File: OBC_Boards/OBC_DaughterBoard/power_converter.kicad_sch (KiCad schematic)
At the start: 12 parts, among them Q1 Q_PMOS_DGS, U2 BU33SA5WGWZ-E2-qsat-symb

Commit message: obc: daughterboard: clean up all schematics for easier reworks
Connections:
- net 3V3: no longer names the net of FB3.1
- net 5V_Rpi_Input: no longer names the net of FB2.2
- net Analog_Voltage: no longer names the net of R7.2, R8.2
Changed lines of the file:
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@@
+    (stroke (width 0) (type default) (color 0 0 0 0))
+  )
+  (wire (pts (xy 101.6 84.455) (xy 109.22 84.455))
     (stroke (width 0) (type default) (color 0 0 0 0))
   )
@@
     (stroke (width 0) (type default) (color 0 0 0 0))
   )
+  (wire (pts (xy 187.96 87.63) (xy 194.945 87.63))
+    (stroke (width 0) (type default) (color 0 0 0 0))
+  )
   (wire (pts (xy 150.114 87.884) (xy 150.114 88.9))
     (stroke (width 0) (type default) (color 0 0 0 0))
@@
   )
   (wire (pts (xy 137.16 95.504) (xy 137.16 98.806))
+    (stroke (width 0) (type default) (color 0 0 0 0))
+  )
+  (wire (pts (xy 194.945 80.01) (xy 194.945 87.63))
     (stroke (width 0) (type default) (color 0 0 0 0))
   )
@@
     (stroke (width 0) (type default) (color 0 0 0 0))
   )
-  (wire (pts (xy 105.918 84.074) (xy 109.22 84.074))
-    (stroke (width 0) (type default) (color 0 0 0 0))
-  )
   (wire (pts (xy 154.686 110.744) (xy 154.686 115.824))
     (stroke (width 0) (type default) (color 0 0 0 0))
   )
   (wire (pts (xy 159.004 91.694) (xy 159.004 94.488))
+    (stroke (width 0) (type default) (color 0 0 0 0))
+  )
+  (wire (pts (xy 101.6 84.455) (xy 101.6 83.82))
     (stroke (width 0) (type default) (color 0 0 0 0))
   )
@@
     (stroke (width 0) (type default) (color 0 0 0 0))
   )
-  (global_label "3V3" (shape input) (at 185.42 87.884 270) (fields_autoplaced)
+  (hierarchical_label "5V0_Input" (shape input) (at 101.6 83.82 180)
     (effects (font (size 1.27 1.27)) (justify right))
-    (property "Intersheet References" "${INTERSHEET_REFS}" (id 0) (at 185.3406 93.8047 90)
-      (effects (font (size 1.27 1.27)) (justify right) hide)
-    )
   )
-  (global_label "5V_Rpi_Input" (shape input) (at 105.918 84.074 180) (fields_autoplaced)
-    (effects (font (size 1.27 1.27)) (justify right))
-    (property "Intersheet References" "${INTERSHEET_REFS}" (id 0) (at 91.4701 83.9946 0)
-      (effects (font (size 1.27 1.27)) (justify right) hide)
-    )
-  )
-  (global_label "Analog_Voltage" (shape input) (at 165.608 110.744 0) (fields_autoplaced)
+  (hierarchical_label "Analog Output Voltage" (shape input) (at 165.735 110.49 0)
     (effects (font (size 1.27 1.27)) (justify left))
-    (property "Intersheet References" "${INTERSHEET_REFS}" (id 0) (at 182.354 110.6646 0)
-      (effects (font (size 1.27 1.27)) (justify left) hide)
-    )
-  )
-  (global_label "PM_Input" (shape input) (at 187.96 87.884 0) (fields_autoplaced)
-    (effects (font (size 1.27 1.27)) (justify left))
-    (property "Intersheet References" "${INTERSHEET_REFS}" (id 0) (at 198.8398 87.8046 0)
-      (effects (font (size 1.27 1.27)) (justify left) hide)
-    )
   )
   (symbol (lib_id "Device:Q_PMOS_DGS") (at 120.396 86.614 90) (unit 1)
@@
     (pin "2")
   )
+  (symbol (lib_id "power:+3V3") (at 194.945 80.01 0) (unit 1)
+    (in_bom yes) (on_board yes) (fields_autoplaced)
+    (property "Reference" "#PWR025" (id 0) (at 194.945 83.82 0)
+      (effects (font (size 1.27 1.27)) hide)
+    )
+    (property "Value" "+3V3" (id 1) (at 194.945 74.93 0))
+    (property "Footprint" "" (id 2) (at 194.945 80.01 0)
+      (effects (font (size 1.27 1.27)) hide)
+    )
+    (property "Datasheet" "" (id 3) (at 194.945 80.01 0)
+      (effects (font (size 1.27 1.27)) hide)
+    )
+    (pin "1")
+  )
   (symbol (lib_id "power:GND") (at 168.656 115.824 0) (unit 1)
     (in_bom yes) (on_board yes) (fields_autoplaced)
@@
   )
   (symbol (lib_id "Device:FerriteBead_Small") (at 111.76 84.074 270) (unit 1)
-    (in_bom yes) (on_board yes) (fields_autoplaced)
-    (property "Reference" "FB2" (id 0) (at 111.7981 77.724 90))
-    (property "Value" "100R @ 100 MHz" (id 1) (at 111.7981 80.264 90))
+    (in_bom yes) (on_board yes)
+    (property "Reference" "FB2" (id 0) (at 102.235 77.47 90))
+    (property "Value" "100R @ 100 MHz" (id 1) (at 106.045 79.375 90))
     (property "Footprint" "Daughterboard_footprints:BEADC1608X75N" (id 2) (at 111.76 82.296 90)
       (effects (font (size 1.27 1.27)) hide)

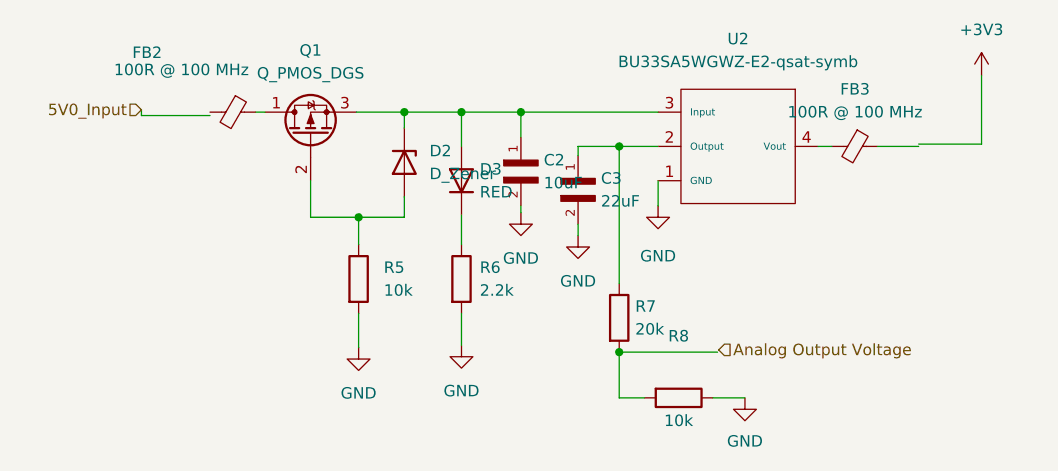
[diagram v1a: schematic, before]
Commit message: footprint fix
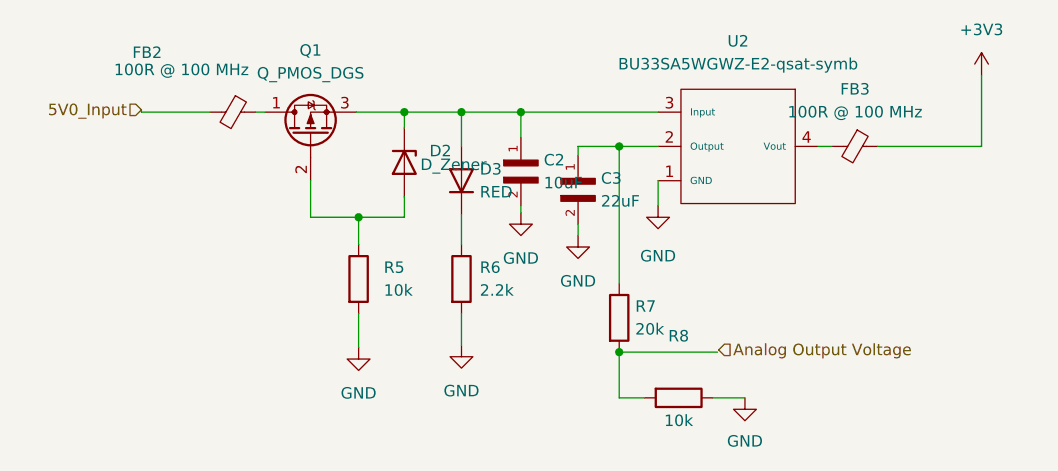
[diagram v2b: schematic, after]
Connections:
- net +3V3: now also FB3.1
- net 5V0_Input: now also FB2.2
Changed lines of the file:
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@@
     (stroke (width 0) (type default) (color 0 0 0 0))
   )
-  (wire (pts (xy 101.6 84.455) (xy 109.22 84.455))
+  (wire (pts (xy 101.6 84.074) (xy 109.22 84.074))
     (stroke (width 0) (type default) (color 0 0 0 0))
   )
@@
     (stroke (width 0) (type default) (color 0 0 0 0))
   )
-  (wire (pts (xy 187.96 87.884) (xy 183.388 87.884))
-    (stroke (width 0) (type default) (color 0 0 0 0))
-  )
-  (wire (pts (xy 187.96 87.63) (xy 194.945 87.63))
+  (wire (pts (xy 183.388 87.884) (xy 194.945 87.884))
     (stroke (width 0) (type default) (color 0 0 0 0))
   )
@@
     (stroke (width 0) (type default) (color 0 0 0 0))
   )
-  (wire (pts (xy 194.945 80.01) (xy 194.945 87.63))
+  (wire (pts (xy 194.945 80.01) (xy 194.945 87.884))
     (stroke (width 0) (type default) (color 0 0 0 0))
   )
@@
     (stroke (width 0) (type default) (color 0 0 0 0))
   )
-  (wire (pts (xy 101.6 84.455) (xy 101.6 83.82))
+  (wire (pts (xy 101.6 84.074) (xy 101.6 83.82))
     (stroke (width 0) (type default) (color 0 0 0 0))
   )
@@
   )
   (symbol (lib_id "Device:D_Zener") (at 130.81 89.662 270) (unit 1)
-    (in_bom yes) (on_board yes) (fields_autoplaced)
-    (property "Reference" "D2" (id 0) (at 133.604 88.3919 90)
-      (effects (font (size 1.27 1.27)) (justify left))
-    )
-    (property "Value" "D_Zener" (id 1) (at 133.604 90.9319 90)
+    (in_bom yes) (on_board yes)
+    (property "Reference" "D2" (id 0) (at 133.604 88.392 90)
+      (effects (font (size 1.27 1.27)) (justify left))
+    )
+    (property "Value" "D_Zener" (id 1) (at 132.588 89.916 90)
       (effects (font (size 1.27 1.27)) (justify left))
     )
@@
   (symbol (lib_id "Imported_OBC_Library:BU33SA5WGWZ-E2-qsat-symb") (at 167.894 87.884 270) (unit 1)
     (in_bom yes) (on_board yes) (fields_autoplaced)
-    (property "Reference" "U2" (id 0) (at 167.894 75.946 90))
-    (property "Value" "BU33SA5WGWZ-E2-qsat-symb" (id 1) (at 167.894 78.486 90))
+    (property "Reference" "U2" (id 0) (at 167.894 76.2 90))
+    (property "Value" "BU33SA5WGWZ-E2-qsat-symb" (id 1) (at 167.894 78.74 90))
     (property "Footprint" "STM32_Breakout:BU33SA5WGWZ-E2" (id 2) (at 167.894 87.884 0)
       (effects (font (size 1.27 1.27)) hide)

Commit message: adding charging circuit
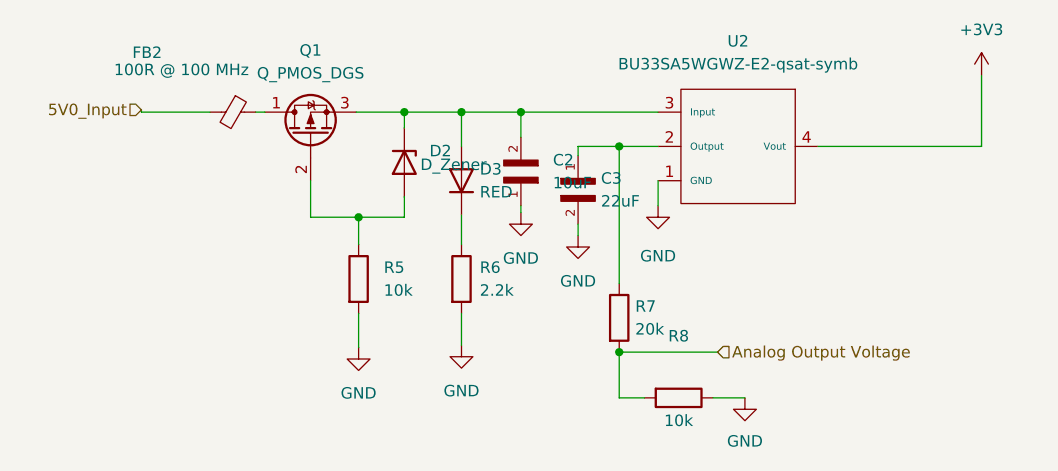
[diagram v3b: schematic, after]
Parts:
- removed FB3: 100R @ 100 MHz, Daughterboard_footprints:BEADC1608X75N, symbol Device:FerriteBead_Small
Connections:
- net +3V3: now also U2.4 (Vout)
- net Analog Output Voltage: now also R7.2, R8.2
- net GND: now also C2.1; no longer C2.2
- net at D2.1 (K), D3.1 (A), Q1.3 (S)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: now also C2.2; no longer C2.1
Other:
- moved on the sheet: C2
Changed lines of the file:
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@@
-    (stroke (width 0) (type default) (color 0 0 0 0))
-  )
-  (wire (pts (xy 183.388 87.884) (xy 194.945 87.884))
     (stroke (width 0) (type default) (color 0 0 0 0))
   )
@@
     (stroke (width 0) (type default) (color 0 0 0 0))
   )
-  (wire (pts (xy 178.308 87.884) (xy 176.784 87.884))
+  (wire (pts (xy 176.784 87.884) (xy 194.945 87.884))
     (stroke (width 0) (type default) (color 0 0 0 0))
   )
@@
     (effects (font (size 1.27 1.27)) (justify right))
   )
-  (hierarchical_label "Analog Output Voltage" (shape input) (at 165.735 110.49 0)
+  (hierarchical_label "Analog Output Voltage" (shape input) (at 165.608 110.744 0)
     (effects (font (size 1.27 1.27)) (justify left))
   )
@@
     (pin "3")
   )
-  (symbol (lib_id "Daughterboard_Symbols:CL10B104KB8NNNL") (at 143.764 89.408 270) (unit 1)
-    (in_bom yes) (on_board yes) (fields_autoplaced)
-    (property "Reference" "C2" (id 0) (at 146.304 89.4079 90)
-      (effects (font (size 1.27 1.27)) (justify left))
-    )
-    (property "Value" "10uF" (id 1) (at 146.304 91.9479 90)
-      (effects (font (size 1.27 1.27)) (justify left))
-    )
-    (property "Footprint" "CAPC1608X90N" (id 2) (at 143.764 89.408 0)
-      (effects (font (size 1.27 1.27)) (justify left bottom) hide)
-    )
-    (property "Datasheet" "" (id 3) (at 143.764 89.408 0)
+  (symbol (lib_id "Daughterboard_Symbols:CL10B104KB8NNNL") (at 143.764 91.948 90) (unit 1)
+    (in_bom yes) (on_board yes) (fields_autoplaced)
+    (property "Reference" "C2" (id 0) (at 147.32 89.4079 90)
+      (effects (font (size 1.27 1.27)) (justify right))
+    )
+    (property "Value" "10uF" (id 1) (at 147.32 91.9479 90)
+      (effects (font (size 1.27 1.27)) (justify right))
+    )
+    (property "Footprint" "CAPC1608X90N" (id 2) (at 143.764 91.948 0)
+      (effects (font (size 1.27 1.27)) (justify left bottom) hide)
+    )
+    (property "Datasheet" "" (id 3) (at 143.764 91.948 0)
       (effects (font (size 1.27 1.27)) (justify left bottom) hide)
     )
@@
     )
     (pin "1")
-    (pin "2")
-  )
-  (symbol (lib_id "Device:FerriteBead_Small") (at 180.848 87.884 270) (unit 1)
-    (in_bom yes) (on_board yes) (fields_autoplaced)
-    (property "Reference" "FB3" (id 0) (at 180.8861 81.534 90))
-    (property "Value" "100R @ 100 MHz" (id 1) (at 180.8861 84.074 90))
-    (property "Footprint" "Daughterboard_footprints:BEADC1608X75N" (id 2) (at 180.848 86.106 90)
-      (effects (font (size 1.27 1.27)) hide)
-    )
-    (property "Datasheet" "~" (id 3) (at 180.848 87.884 0)
-      (effects (font (size 1.27 1.27)) hide)
-    )
-    (pin "1")

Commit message: Layout completed
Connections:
- net +3V3 renamed VCC_3V3
- net 5V0_Input renamed +5V
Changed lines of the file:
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@@
+    (stroke (width 0) (type default) (color 0 0 0 0))
+  )
+  (wire (pts (xy 176.784 87.63) (xy 176.784 87.884))
     (stroke (width 0) (type default) (color 0 0 0 0))
   )
@@
     (stroke (width 0) (type default) (color 0 0 0 0))
   )
-  (wire (pts (xy 194.945 80.01) (xy 194.945 87.884))
-    (stroke (width 0) (type default) (color 0 0 0 0))
-  )
-  (wire (pts (xy 176.784 87.884) (xy 194.945 87.884))
+  (wire (pts (xy 176.784 87.63) (xy 185.42 87.757))
     (stroke (width 0) (type default) (color 0 0 0 0))
   )
@@
     (stroke (width 0) (type default) (color 0 0 0 0))
   )
-  (hierarchical_label "5V0_Input" (shape input) (at 101.6 83.82 180)
-    (effects (font (size 1.27 1.27)) (justify right))
+  (hierarchical_label "VCC_3V3" (shape input) (at 185.42 87.757 0)
+    (effects (font (size 1.27 1.27)) (justify left))
   )
   (hierarchical_label "Analog Output Voltage" (shape input) (at 165.608 110.744 0)
@@
     (pin "2")
   )
-  (symbol (lib_id "power:+3V3") (at 194.945 80.01 0) (unit 1)
-    (in_bom yes) (on_board yes) (fields_autoplaced)
-    (property "Reference" "#PWR025" (id 0) (at 194.945 83.82 0)
-      (effects (font (size 1.27 1.27)) hide)
-    )
-    (property "Value" "+3V3" (id 1) (at 194.945 74.93 0))
-    (property "Footprint" "" (id 2) (at 194.945 80.01 0)
-      (effects (font (size 1.27 1.27)) hide)
-    )
-    (property "Datasheet" "" (id 3) (at 194.945 80.01 0)
-      (effects (font (size 1.27 1.27)) hide)
-    )
-    (pin "1")
-  )
   (symbol (lib_id "power:GND") (at 168.656 115.824 0) (unit 1)
     (in_bom yes) (on_board yes) (fields_autoplaced)
@@
     (pin "2")
   )
+  (symbol (lib_id "power:+5V") (at 101.6 83.82 0) (unit 1)
+    (in_bom yes) (on_board yes) (fields_autoplaced)
+    (property "Reference" "#PWR0127" (id 0) (at 101.6 87.63 0)
+      (effects (font (size 1.27 1.27)) hide)
+    )
+    (property "Value" "+5V" (id 1) (at 101.6 78.74 0))
+    (property "Footprint" "" (id 2) (at 101.6 83.82 0)
+      (effects (font (size 1.27 1.27)) hide)
+    )
+    (property "Datasheet" "" (id 3) (at 101.6 83.82 0)
+      (effects (font (size 1.27 1.27)) hide)
+    )
+    (pin "1")
+  )
   (symbol (lib_id "power:GND") (at 150.114 97.79 0) (unit 1)
